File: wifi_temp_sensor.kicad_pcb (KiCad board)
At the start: 2 copper layers, 50.2 x 33 mm, 9 parts, among them J1 USB_B_Mini, J2 Conn_02x04_Odd_Even, J3 Conn_01x04, J4 Conn_01x06, J6 Conn_01x01, J8 Conn_01x01, SW1 SW_DIP_x01

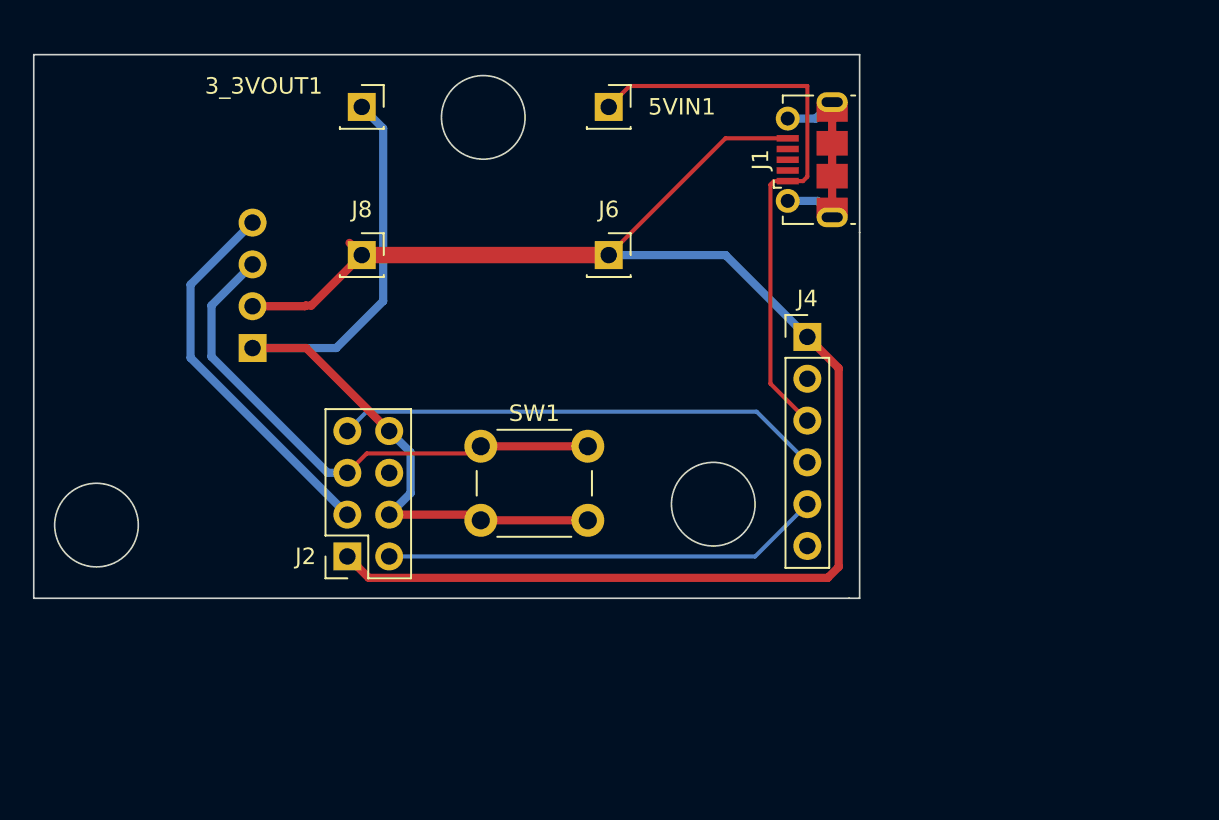
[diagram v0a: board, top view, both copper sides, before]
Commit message: Fixed minor issues and re-did the PCB
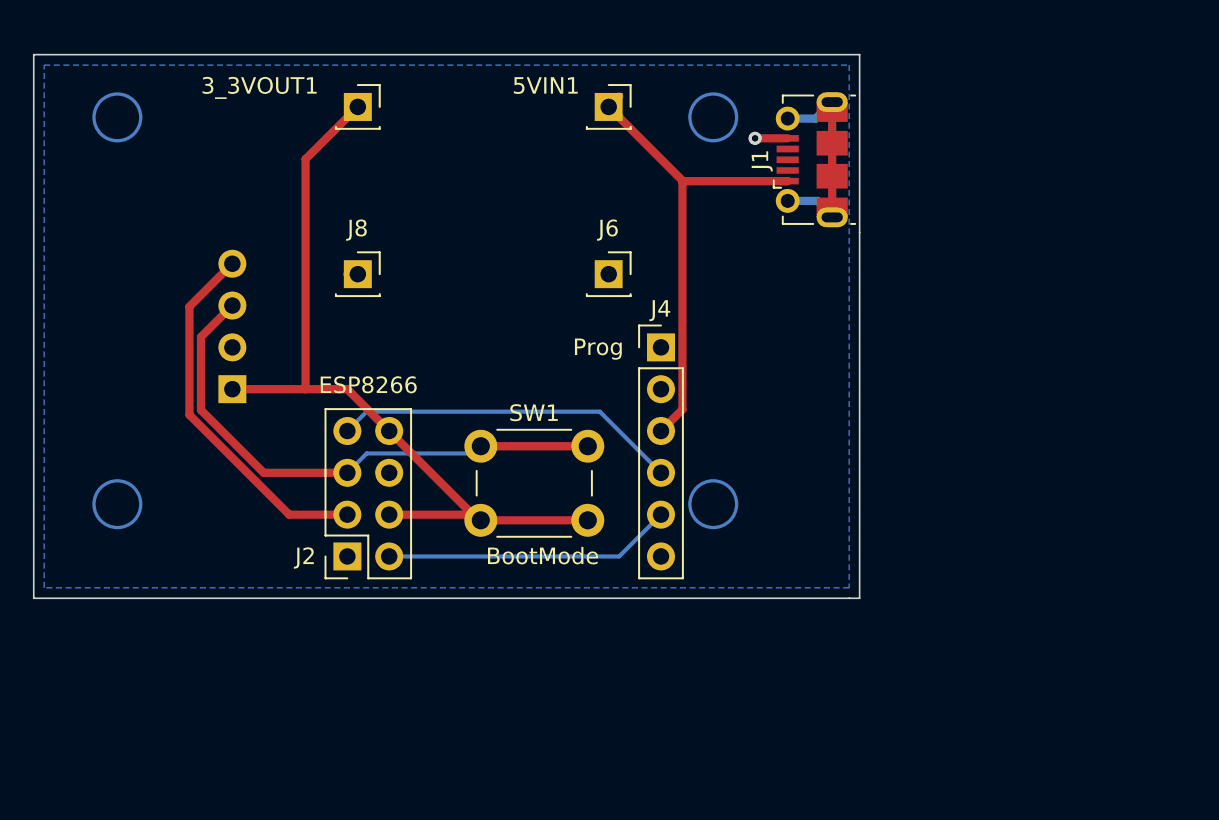
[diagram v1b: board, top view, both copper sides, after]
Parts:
- J2: value Conn_02x04_Odd_Even -> ESP8266
- J3: value Conn_01x04 -> TempSensor
- J4: value Conn_01x06 -> Prog
- SW1: value SW_DIP_x01 -> BootMode
- moved J4 8.91 mm to (202.6, 43.8)
- moved J3 2.78 mm to (176.5, 46.4)
- moved J8 1.18 mm to (184.2, 39.4)
- moved J6 1.16 mm to (199.4, 39.4)
- moved 3_3VOUT1 0.24 mm to (184.2, 29.2)
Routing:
- net GND: track 98.0 -> 2.62 mm, vias 0 -> 1
- net ESP_Tx: track 26.7 -> 17.6 mm
- net ESP_Rx: track 29.7 -> 21.1 mm
- net +5V: track 35.8 -> 29.8 mm
- net +3.3V: track 50.7 -> 49.5 mm
- net SDA: track 23.2 -> 22.4 mm
- added copper zone on B.Cu, net GND
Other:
- outline, holes or cut-outs redrawn

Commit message: minor fix
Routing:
- net SCL: track 33.5 -> 32.6 mm
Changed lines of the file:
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@@
   (gr_line (start 213.995 59.055) (end 214.63 59.055)
     (stroke (width 0.1) (type default)) (layer "Edge.Cuts"))
-  (segment (start 180.975 32.385) (end 180.975 46.355) (width 0.5) (layer "F.Cu") (net 1))
   (segment (start 191.62 54.32) (end 198.12 54.32) (width 0.5) (layer "F.Cu") (net 1))
   (segment (start 191.48 54.32) (end 191.62 54.32) (width 0.5) (layer "F.Cu") (net 1))
+  (segment (start 180.975 46.355) (end 176.53 46.355) (width 0.5) (layer "F.Cu") (net 1))
+  (segment (start 186.055 53.975) (end 191.275 53.975) (width 0.5) (layer "F.Cu") (net 1))
+  (segment (start 180.975 32.385) (end 180.975 46.355) (width 0.5) (layer "F.Cu") (net 1))
+  (segment (start 186.055 48.895) (end 183.515 46.355) (width 0.5) (layer "F.Cu") (net 1))
   (segment (start 184.15 29.21) (end 180.975 32.385) (width 0.5) (layer "F.Cu") (net 1))
-  (segment (start 186.055 53.975) (end 191.275 53.975) (width 0.5) (layer "F.Cu") (net 1))
-  (segment (start 186.055 48.895) (end 183.515 46.355) (width 0.5) (layer "F.Cu") (net 1))
-  (segment (start 180.975 46.355) (end 176.53 46.355) (width 0.5) (layer "F.Cu") (net 1))
   (segment (start 191.275 53.975) (end 191.62 54.32) (width 0.5) (layer "F.Cu") (net 1))
   (segment (start 186.055 48.895) (end 191.48 54.32) (width 0.5) (layer "F.Cu") (net 1))
@@
   (segment (start 202.565 53.975) (end 200.025 56.515) (width 0.25) (layer "B.Cu") (net 8))
   (segment (start 200.025 56.515) (end 186.055 56.515) (width 0.25) (layer "B.Cu") (net 8))
-  (segment (start 173.925 41.34) (end 176.53 38.735) (width 0.5) (layer "F.Cu") (net 9))
-  (segment (start 173.925 47.914949) (end 173.925 41.34) (width 0.5) (layer "F.Cu") (net 9))
-  (segment (start 179.98505 53.975) (end 173.925 47.914949) (width 0.5) (layer "F.Cu") (net 9))
-  (segment (start 183.515 53.975) (end 179.98505 53.975) (width 0.5) (layer "F.Cu") (net 9))
-  (segment (start 174.625 47.625) (end 174.625 43.18) (width 0.5) (layer "F.Cu") (net 10))
+  (segment (start 183.515 53.975) (end 180.686572 53.975) (width 0.5) (layer "F.Cu") (net 9))
+  (segment (start 180.686572 53.975) (end 173.99 47.278428) (width 0.5) (layer "F.Cu") (net 9))
+  (segment (start 173.99 47.278428) (end 173.99 41.275) (width 0.5) (layer "F.Cu") (net 9))
+  (segment (start 173.99 41.275) (end 176.53 38.735) (width 0.5) (layer "F.Cu") (net 9))
   (segment (start 191.62 49.82) (end 191.18 50.26) (width 0.25) (layer "F.Cu") (net 10))
-  (segment (start 174.625 43.18) (end 176.53 41.275) (width 0.5) (layer "F.Cu") (net 10))
-  (segment (start 183.515 51.435) (end 178.435 51.435) (width 0.5) (layer "F.Cu") (net 10))
-  (segment (start 178.435 51.435) (end 174.625 47.625) (width 0.5) (layer "F.Cu") (net 10))
+  (segment (start 175.23 47.528478) (end 179.136522 51.435) (width 0.5) (layer "F.Cu") (net 10))
+  (segment (start 176.53 41.275) (end 175.23 42.575) (width 0.5) (layer "F.Cu") (net 10))
   (segment (start 191.62 49.82) (end 198.12 49.82) (width 0.5) (layer "F.Cu") (net 10))
+  (segment (start 179.136522 51.435) (end 183.515 51.435) (width 0.5) (layer "F.Cu") (net 10))
+  (segment (start 175.23 42.575) (end 175.23 47.528478) (width 0.5) (layer "F.Cu") (net 10))
   (segment (start 184.69 50.26) (end 191.18 50.26) (width 0.25) (layer "B.Cu") (net 10))
   (segment (start 191.18 50.26) (end 191.62 49.82) (width 0.25) (layer "B.Cu") (net 10))

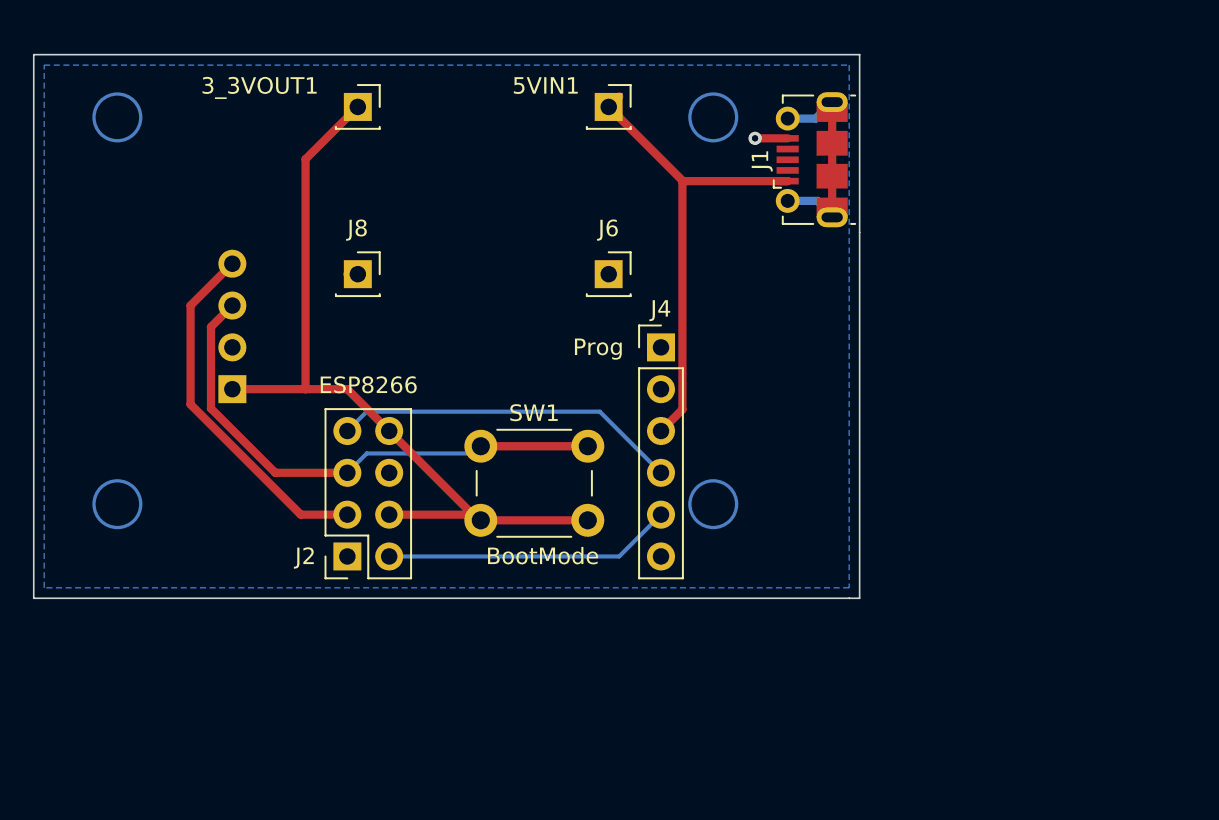
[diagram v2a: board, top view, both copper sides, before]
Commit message: Resized board and added LDO PSU
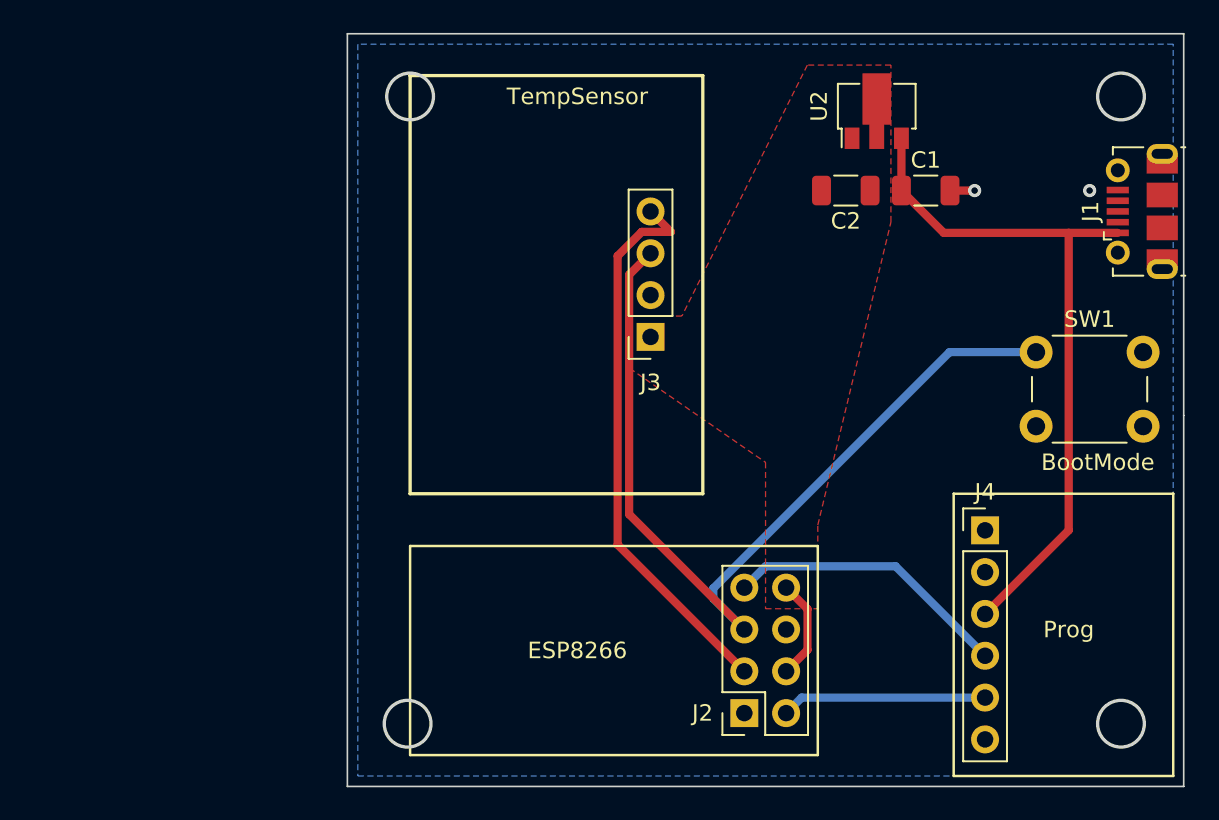
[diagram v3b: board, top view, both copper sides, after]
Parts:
- removed 3_3VOUT1, 5VIN1, J6, J8: Conn_01x01, Connector_PinSocket_2.54mm:PinSocket_1x01_P2.54mm_Vertical
- added C1: C_Small, Capacitor_SMD:C_1206_3216Metric, F.Cu at (218.6, 34.3)
- added C2: C_Small, Capacitor_SMD:C_1206_3216Metric, F.Cu at (213.8, 34.3)
- added U2: AZ1117-3.3, Package_TO_SOT_SMD:SOT-89-3, F.Cu at (215.7, 29.2)
- J3: footprint Connector_PinSocket_2.54mm:PinSocket_1x04_P2.54mm_Horizontal -> Connector_PinSocket_2.54mm:PinSocket_1x04_P2.54mm_Vertical; moved to F.Cu
- moved SW1 34.2 mm to (225.3, 44.1)
- moved J2 25.9 mm to (207.6, 66.0)
- moved J3 25.6 mm to (201.9, 43.2), turned to 180 degrees
- moved J4 22.6 mm to (222.2, 54.9)
- moved J1 20.3 mm to (231.8, 35.6)
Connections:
- SW1 pad 2: +3.3V -> GND
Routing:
- net +3.3V: track 49.5 -> 6.16 mm
- net SCL: track 32.6 -> 55.1 mm
- net +5V: track 29.8 -> 42.6 mm
- net SDA: track 21.9 -> 34.0 mm
- net unconnected-(J1-Shield-Pad6): track 12.1 -> 0.00 mm
- net ESP_Tx: track 17.6 -> 12.5 mm
- net ESP_Rx: track 21.1 -> 17.4 mm
- net GND: track 2.62 -> 1.50 mm, vias 1 -> 2
- added copper zone on F.Cu, net +3.3V
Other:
- board size 50.2 x 33 mm -> 50.8 x 45.7 mm

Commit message: updates
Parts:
- moved J1 0.64 mm to (231.1, 35.6)
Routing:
- net SCL: track 55.1 -> 61.6 mm
- net GND: track 1.50 -> 3.22 mm
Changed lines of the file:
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@@
     (property "ki_keywords" "connector")
     (attr through_hole)
-    (fp_text reference "J4" (at 0 -2.33) (layer "F.SilkS")
+    (fp_text reference "J4" (at -0.635 -3.4925) (layer "F.SilkS")
         (effects (font (size 1 1) (thickness 0.15)))
     )
@@
   )
   (footprint "Connector_USB:USB_Micro-B_Molex-105017-0001" (layer "F.Cu")
-    (at 231.775 35.56 90)
+    (at 231.14 35.56 90)
     (descr "http://www.molex.com/pdm_docs/sd/1050170001_sd.pdf")
     (tags "Micro-USB SMD Typ-B")
@@
     )
   )
-  (gr_rect (start 187.325 27.305) (end 205.105 52.705)
+  (gr_rect (start 189.23 27.305) (end 205.105 52.705)
     (stroke (width 0.2) (type default)) (fill none) (layer "F.SilkS"))
   (gr_rect (start 220.345 52.705) (end 233.68 69.85)
     (stroke (width 0.15) (type default)) (fill none) (layer "F.SilkS"))
-  (gr_rect (start 187.325 55.88) (end 212.09 68.58)
+  (gr_rect (start 189.23 55.88) (end 212.09 68.58)
     (stroke (width 0.15) (type default)) (fill none) (layer "F.SilkS"))
   (gr_line (start 234.315 47.9425) (end 234.315 24.765)
@@
   (segment (start 219.74 36.86) (end 217.17 34.29) (width 0.5) (layer "F.Cu") (net 2))
   (segment (start 227.33 36.86) (end 219.74 36.86) (width 0.5) (layer "F.Cu") (net 2))
+  (segment (start 229.6775 34.26) (end 227.995 34.26) (width 0.5) (layer "F.Cu") (net 6))
+  (segment (start 227.995 34.26) (end 227.965 34.29) (width 0.5) (layer "F.Cu") (net 6))
   (segment (start 220.12 34.29) (end 221.615 34.29) (width 0.5) (layer "F.Cu") (net 6))
-  (via (at 228.6 34.29) (size 0.8) (drill 0.4) (layers "F.Cu" "B.Cu") (free) (net 6))
+  (via (at 227.965 34.29) (size 0.8) (drill 0.4) (layers "F.Cu" "B.Cu") (free) (net 6))
   (via (at 221.615 34.29) (size 0.8) (drill 0.4) (layers "F.Cu" "B.Cu") (free) (net 6))
   (segment (start 211.1075 65.0875) (end 222.25 65.0875) (width 0.5) (layer "B.Cu") (net 8))
@@
   (segment (start 225.35 44.105) (end 220.091522 44.105) (width 0.5) (layer "B.Cu") (net 10))
   (segment (start 205.74 58.456522) (end 205.74 59.065) (width 0.5) (layer "B.Cu") (net 10))
+  (segment (start 225.35 44.105) (end 231.85 44.105) (width 0.5) (layer "B.Cu") (net 10))
   (segment (start 220.091522 44.105) (end 205.74 58.456522) (width 0.5) (layer "B.Cu") (net 10))
   (segment (start 208.925 57.11) (end 216.8125 57.11) (width 0.5) (layer "B.Cu") (net 12))
